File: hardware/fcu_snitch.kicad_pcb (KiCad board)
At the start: 6 copper layers, 53.5 x 46 mm, 106 parts, among them J1 Conn_01x04_Socket, J2 Conn_01x02_Socket, J3 Conn_02x04_Top_Bottom, J4 SMA, J5 02x03_SMD, Q1 NPN, U1 LSM6DSO32, U2 LPS22HBTR, U3 BALFHB-WL-05D3, U4 SKY13373-460LF, U5 SN74LVC1G3157DBVR, Y1 ABS07L-32.768KHZ-T, Y2 ASTX-H11

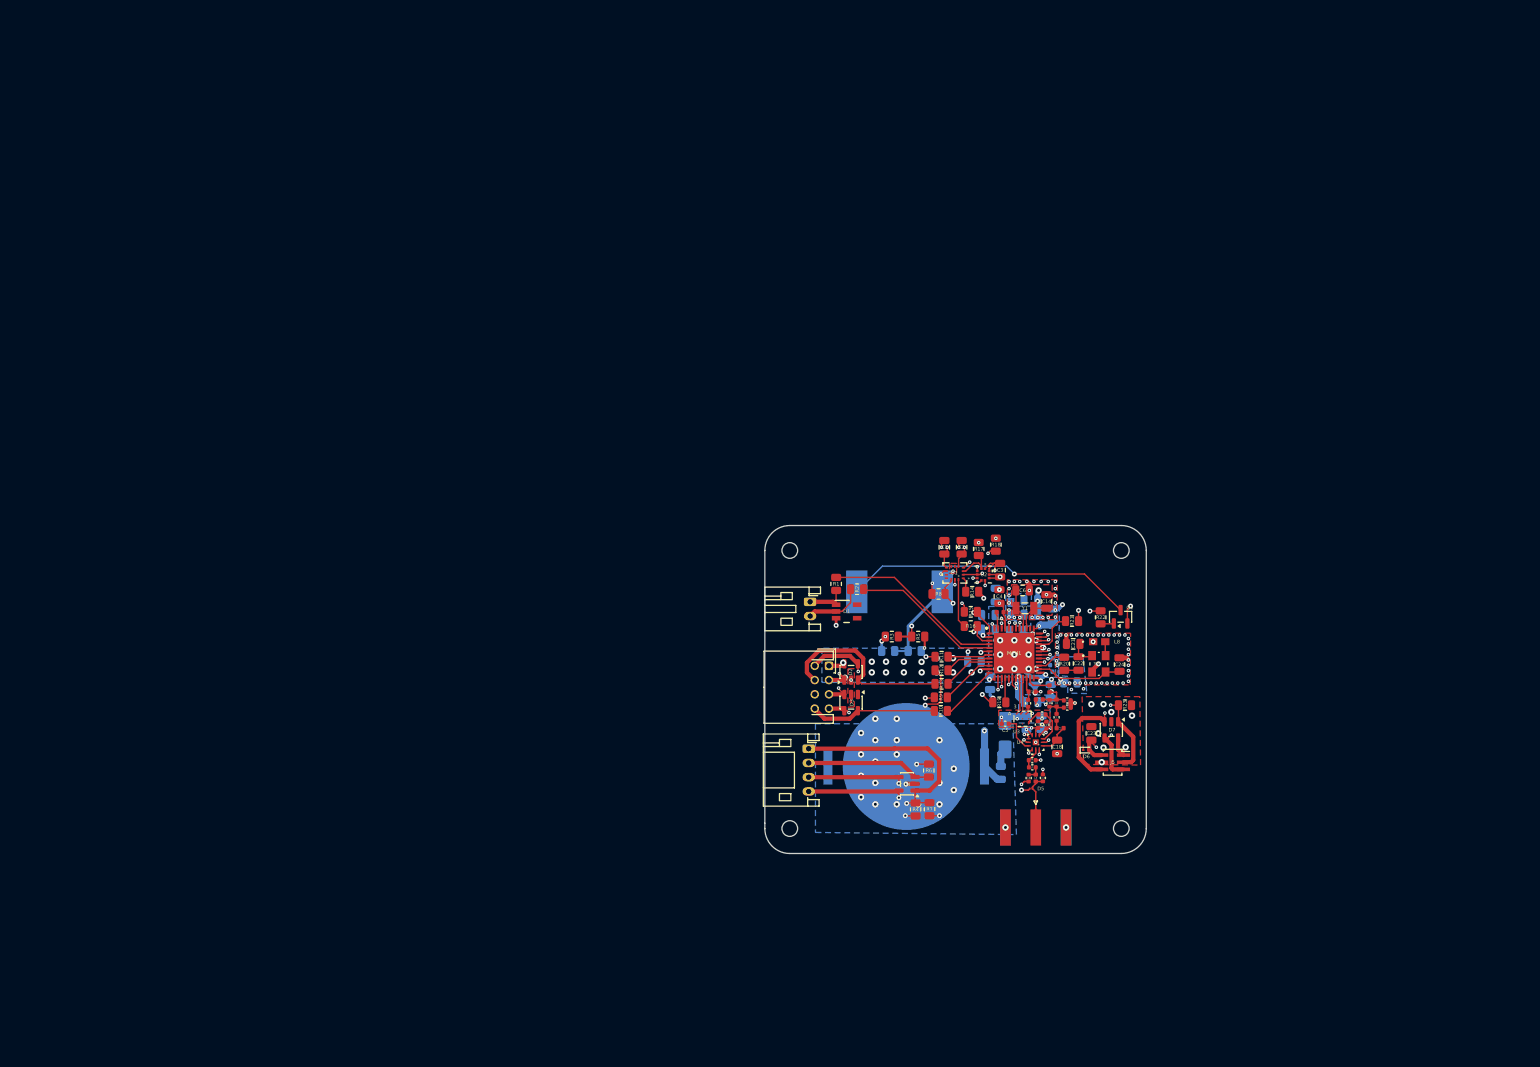
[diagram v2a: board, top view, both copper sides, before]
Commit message: pcb v2 update: test points, stickers, labeling
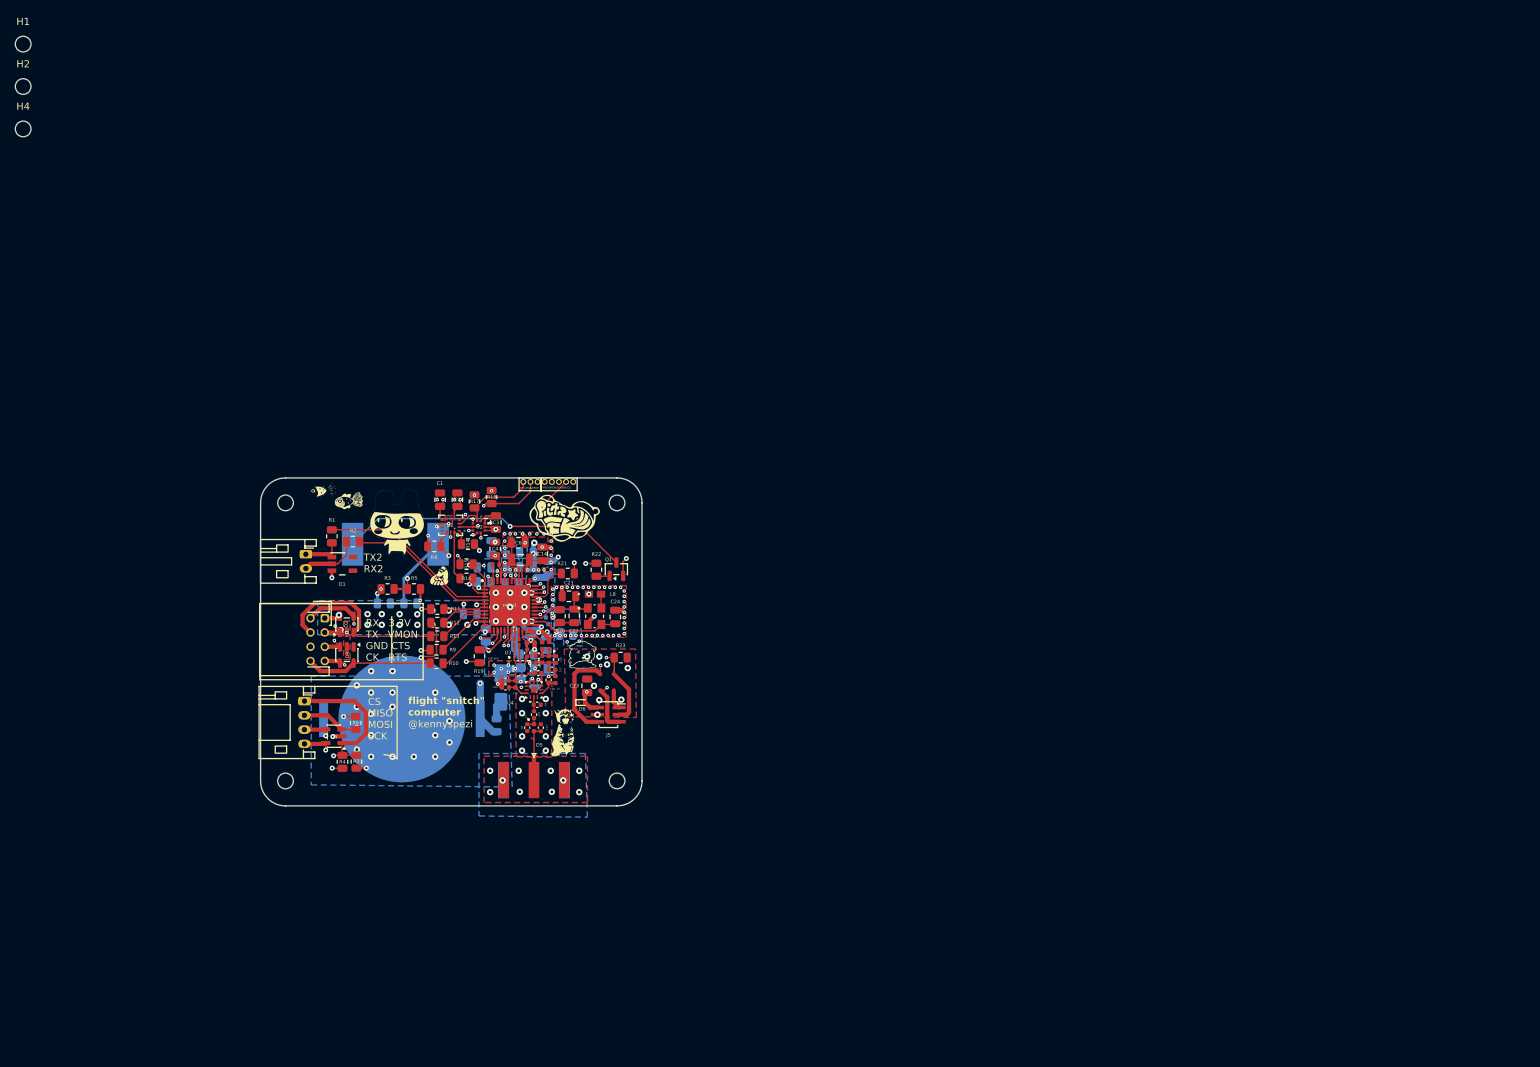
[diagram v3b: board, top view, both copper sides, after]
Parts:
- removed D7: ESDS304, Package_TO_SOT_SMD:SOT-23-5
- added C43: 8p, Capacitor_SMD:C_0402_1005Metric, F.Cu at (70.1, 92.7)
- added G***: LOGO, LOGO, F.Cu at (78.3, 69.2)
- added G***: LOGO, LOGO, B.Cu at (43.4, 78.5)
- added G***: LOGO, LOGO, B.Cu at (43.2, 66.9)
- added G***: LOGO, LOGO, B.Cu at (74.6, 98.3)
- added G***: LOGO, LOGO, B.Cu at (43.2, 70.4)
- added G***: LOGO, LOGO, F.Cu at (78.3, 98.9)
- added G***: LOGO, LOGO, F.Cu at (60.8, 77.0)
- added G***: LOGO, LOGO, F.Cu at (54.9, 69.6)
- added G***: LOGO, LOGO, F.Cu at (80.9, 88.1)
- added G***: LOGO, LOGO, F.Cu at (48.2, 66.5)
- added G***: LOGO, LOGO, F.Cu at (44.4, 65.1)
- added G***: LOGO, LOGO, B.Cu at (83.2, 95.3)
- added G***: LOGO, LOGO, B.Cu at (83.7, 77.9)
- added H1: MountingHole, MountingHole:MountingHole_2.2mm_M2, F.Cu at (2.48, 2.48)
- added H2: MountingHole, MountingHole:MountingHole_2.2mm_M2, F.Cu at (2.48, 8.43)
- added H4: MountingHole, MountingHole:MountingHole_2.2mm_M2, F.Cu at (2.48, 14.4)
- added J6: Conn_01x08_Socket, Connector_PinHeader_1.00mm:PinHeader_1x08_P1.00mm_Horizontal, F.Cu at (72.6, 63.9)
- added L10: 3.6n, Inductor_SMD:L_0402_1005Metric, F.Cu at (71.5, 92.2)
- added R28: R_Small_US, Resistor_SMD:R_0201_0603Metric_Pad0.64x0.40mm_HandSolder, F.Cu at (71.3, 86.4)
- added R29: R_Small_US, Resistor_SMD:R_0201_0603Metric_Pad0.64x0.40mm_HandSolder, F.Cu at (72.0, 86.4)
- C11, C15: moved to B.Cu
- C18: footprint Capacitor_SMD:C_0805_2012Metric -> Capacitor_SMD:C_0402_1005Metric
- J5: value 02x03_SMD -> 02x03_JST_SWD
- moved D4 80.7 mm to (46.0, 99.5)
- moved R4 80.7 mm to (47.3, 103.1)
- moved R6 80.7 mm to (49.1, 97.7)
- moved R7 80.7 mm to (49.2, 103.1)
- moved C20 74.4 mm to (74.8, 89.2), turned to 180 degrees
- moved C19 74.4 mm to (74.8, 88.3), turned to 180 degrees
- moved R19 73.2 mm to (66.5, 88.3), turned to -90 degrees
- moved C18 71.9 mm to (76.2, 91.6), turned to 90 degrees
- moved C15 71.5 mm to (74.8, 92.1), turned to -90 degrees
- moved L6 71.5 mm to (76.2, 88.8)
- moved L5 71.4 mm to (75.3, 86.8)
- moved R24 71.3 mm to (72.3, 90.7)
- moved C11 71.3 mm to (73.8, 92.1), turned to -90 degrees
- moved L7 71.1 mm to (77.1, 91.6), turned to 90 degrees
- moved C17 71.1 mm to (76.6, 90.2), turned to 180 degrees
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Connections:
- net /STM32WLE5 + Radio/IMU_{MISO} renamed /IMU_{MISO}
- net /STM32WLE5 + Radio/IMU_{SCK} renamed /IMU_{SCK}
- C5 pad 2: Net-(U3-J2) -> Net-(U3-RFI_IN)
- MCU1 pad 20: /STM32WLE5 + Radio/RFI_P -> /STM32WLE5 + Radio/mcuRFI_P
- MCU1 pad 21: /STM32WLE5 + Radio/RFI_N -> /STM32WLE5 + Radio/mcuRFI_N
- U3 pad C3: Net-(U3-J2) -> Net-(U3-RFI_IN)
- U4 pad 9: Net-(U3-J2) -> Net-(U4-J2)
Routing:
- net /IMU_CS: track 14.0 -> 41.6 mm
- net /IMU_{SCK}: track 3.76 -> 21.5 mm, vias 0 -> 1
- net /IMU_MOSI: track 6.86 -> 23.8 mm, vias 0 -> 2
- net /IMU_{MISO}: track 7.47 -> 21.8 mm
- net /DRDY: track 8.57 -> 20.2 mm
- net GND: track 51.5 -> 39.9 mm, vias 85 -> 93
- net /SPI2MISO: track 18.0 -> 8.31 mm
- net /STM32WLE5 + Radio/SPI2_{MISO}: track 18.9 -> 27.9 mm
- net /HSCL: track 5.56 -> 14.3 mm
- net /HSDA: track 7.10 -> 14.8 mm
- net /IMU_INT: track 28.6 -> 35.9 mm, vias 2 -> 3
- net Net-(U3-J2): track 5.27 -> 0.00 mm
- net /SPI2SCK: track 35.0 -> 30.8 mm
- net Net-(U4-J2): track 0.00 -> 2.84 mm
- net Net-(MCU1-PA6): track 11.0 -> 13.8 mm
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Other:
- board text added: "@kennyspezi"
- board text added: "CS MISO MOSI SCK"
- board text added: "Calculated CWG Trace Width: 0.19734 mm Calculated Microstrip Trace Width: 0.21567 mm f = 915 Hz (LoRa)"
- board text added: "HCL|HDA|DRDY"
- board text added: "MISO|MOSI|SCK|INT|CS"
- board text added: "RX 3.3V TX VMON GND CTS CK RTS"
- board text added: "TX2 RX2"
- board text added: "flight {dblquote}snitch{dblquote} computer"
- board text added: "test gnd"
- board text added: "well, well, what do we have here ?? ;)"
